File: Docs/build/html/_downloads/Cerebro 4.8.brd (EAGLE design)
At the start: 17.3 x 18.8 mm, 30 parts, among them IC1 OPA237N, T1 FJX3904TF

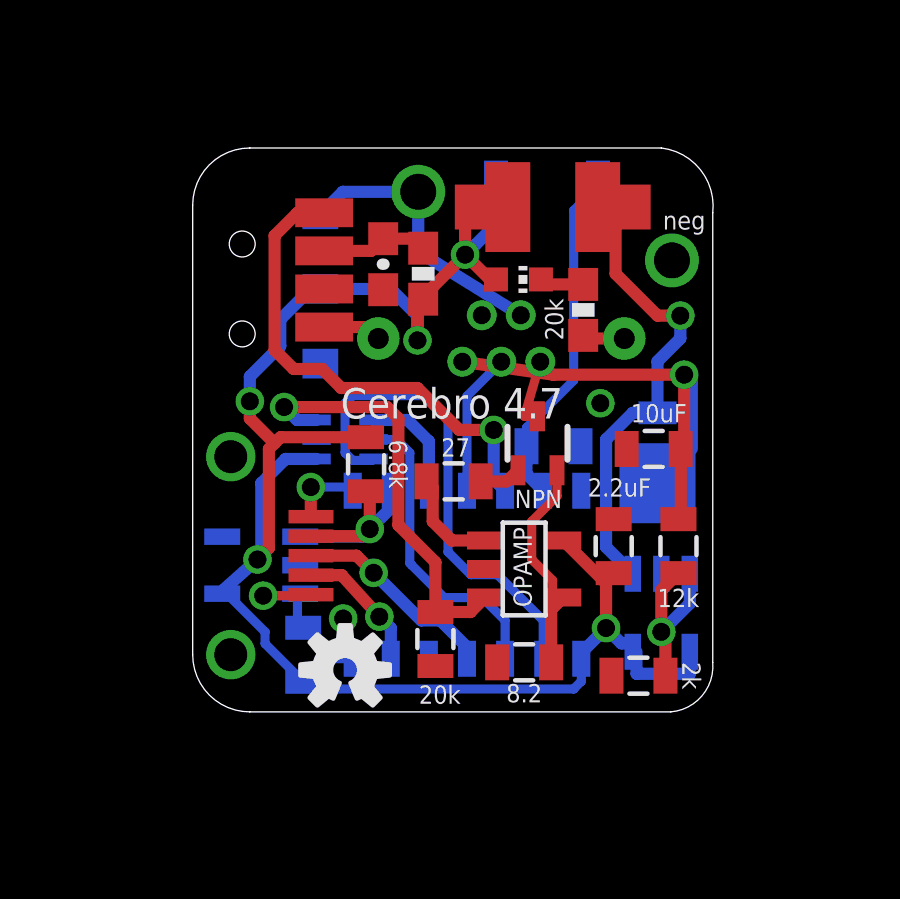
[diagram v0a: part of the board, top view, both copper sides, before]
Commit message: Cerebro PCB update to 4.8: - npn emitter resistor was 8.2ohm, now 6.8 ohm - removed push button resistor and changed to internal pullup resistor on MCU - switched to from 0805 to 0603 for all resistors and capacitors - switched to reinforced microUSB socket - enlarged ground pads on usb plug for stronger solder anchor - added indicator LED to pin 5 (PB2)
Updated cerebro.ino:
- pushbutton now gives a low signal when pressed.
- Arduino IDE update to 1.6.11 effected the delayMicroseconds(), thereby breaking the IR communication. Changed the irResolution to 4 in order to fix.

Updated docs to have Cerebro 4.8 files
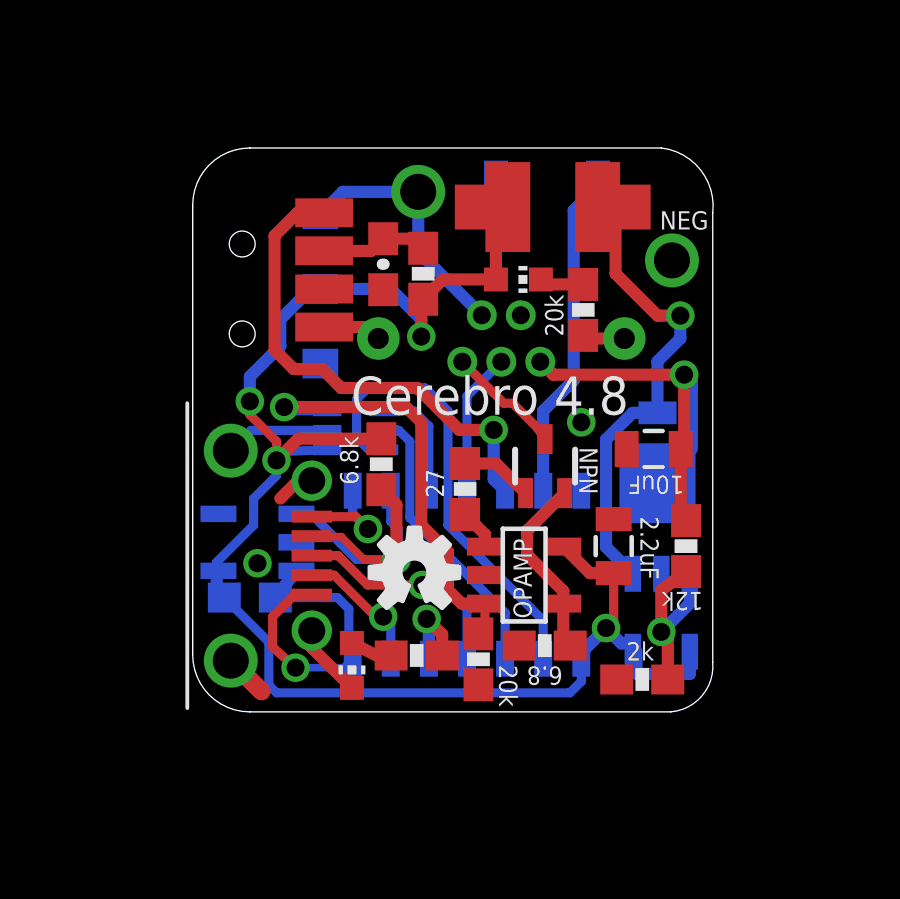
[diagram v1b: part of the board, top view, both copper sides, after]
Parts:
- removed U$5: USB_SOCKET_MICRO_VERTHORIZONTAL, Andy-library:USB_HORZ_MICRO_SMD
- added INDICATOR_LED1: LED, led:CHIP-LED0603
- added SERIAL_SOCKET: USB_SOCKET_MICRO_VERTREINFORCED, Andy-library:USB_HORZ_REINFORCED_MICRO
- R1, R3, R4, R6, R7, R8: device Andy-library:0805 -> Andy-library:0603-RES
- R2: value 8.2 -> 6.8; device Andy-library:0805 -> Andy-library:0603-RES
- R9: value 12k -> 20k; device Andy-library:0805 -> Andy-library:0603-RES
- moved R9 8.33 mm to (7.59, 1.88), flipped to the top, turned to 180 degrees
- moved U$6 3.99 mm to (7.52, 4.65)
- moved R7 2.61 mm to (2.03, 3.81), turned to 0 degrees
- moved R8 1.59 mm to (9.65, 1.75)
- moved R2 0.88 mm to (11.9, 2.21)
- moved T1 0.80 mm to (11.9, 8.19)
- moved U$4 0.77 mm to (2.29, 5.65)
- moved R6 0.51 mm to (6.41, 8.26)
- moved U$1 0.47 mm to (5.56, 9.39)
- moved R1 0.46 mm to (9.21, 7.43), turned to 270 degrees
- moved R4 0.25 mm to (16.6, 5.52)
- moved IC1 0.20 mm to (11.2, 4.56)
- moved R3 0.18 mm to (15.1, 1.08)
- renumbered JP3 to LASER_OUTPUT, U$7 to GROUND
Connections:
- new net N$17: LASER_OUTPUT.1, T1.1
- new net N$18: INDICATOR_LED1.A, R9.2
- net 8.68VDC: now also LASER_OUTPUT.5; no longer LASER_OUTPUT.1
- net BATT: no longer U$3.P$2
- net GND: now also INDICATOR_LED1.C, LASER_OUTPUT.4, SERIAL_SOCKET.G1, SERIAL_SOCKET.G2, SERIAL_SOCKET.P$1, SERIAL_SOCKET.P$2, U$3.P$2; no longer LASER_OUTPUT.2, R9.1, U$5.G1, U$5.G2
- net MISO/TX: now also SERIAL_SOCKET.P1; no longer U$5.P1
- net MOSI: now also SERIAL_SOCKET.P5; no longer U$5.P5
- net N$13: now also R9.1, U$2.5; no longer LASER_OUTPUT.5, T1.1
- net N$4: now also LASER_OUTPUT.2; no longer LASER_OUTPUT.4
- net N$7: no longer R9.2
- net RESET: now also SERIAL_SOCKET.P3; no longer U$5.P3
- net RX: now also SERIAL_SOCKET.P4; no longer U$5.P4
- net SCK: now also SERIAL_SOCKET.P2; no longer U$5.P2
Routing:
- net GND: track 3.38 -> 12.1 mm
- net SCK: track 7.43 -> 12.1 mm
- net MOSI: track 6.62 -> 11.1 mm
- net BATT: track 60.2 -> 55.8 mm, vias 5 -> 4
- net N$17: track 0.00 -> 3.87 mm
- net 8.68VDC: track 17.2 -> 14.9 mm
- net N$9: track 3.42 -> 1.34 mm
- net N$18: track 0.00 -> 1.50 mm
- net N$6: track 7.56 -> 6.33 mm
- net MISO/TX: track 2.52 -> 3.61 mm
- net N$11: track 1.40 -> 2.43 mm
- net N$4: track 9.59 -> 8.57 mm
- net N$16: track 16.4 -> 15.5 mm
- net N$14: track 10.3 -> 9.57 mm
- net RESET: track 6.85 -> 7.57 mm
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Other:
- board text added: "Cerebro 4.8"
- board text added: "NEG"
- board text removed: "Cerebro 4.7"
- board text removed: "neg"
